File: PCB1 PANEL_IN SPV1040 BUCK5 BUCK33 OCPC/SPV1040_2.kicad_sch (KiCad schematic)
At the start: 14 parts, among them J2 SOLAR, U2 SPV1040TTR

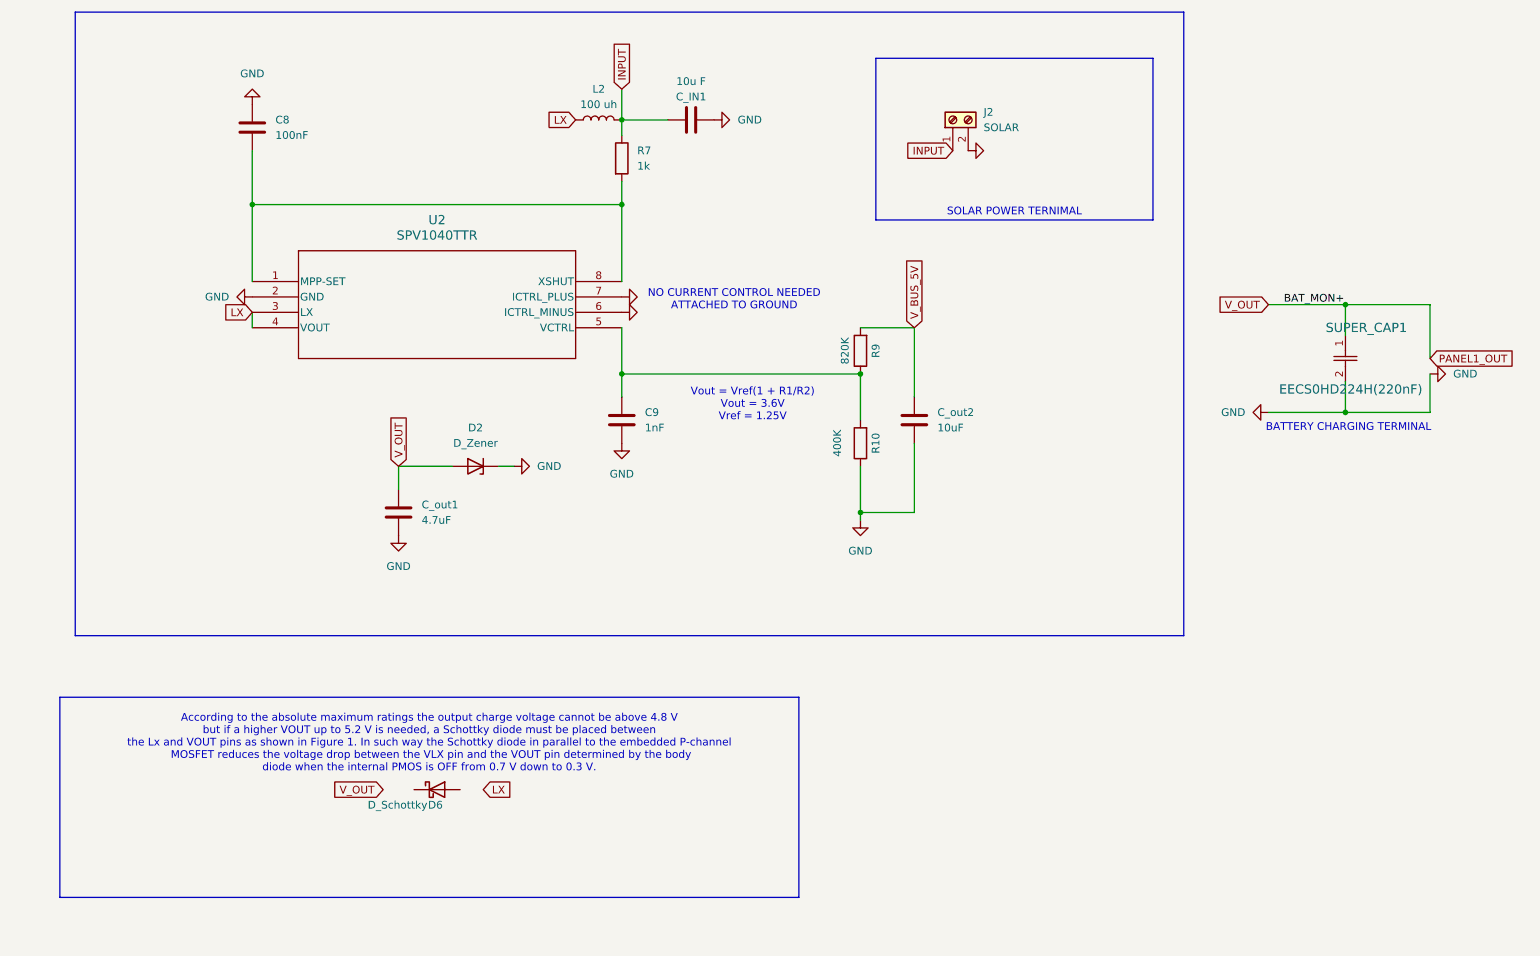
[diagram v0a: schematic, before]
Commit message: Changes
Added bucks from old work
and copied SPV
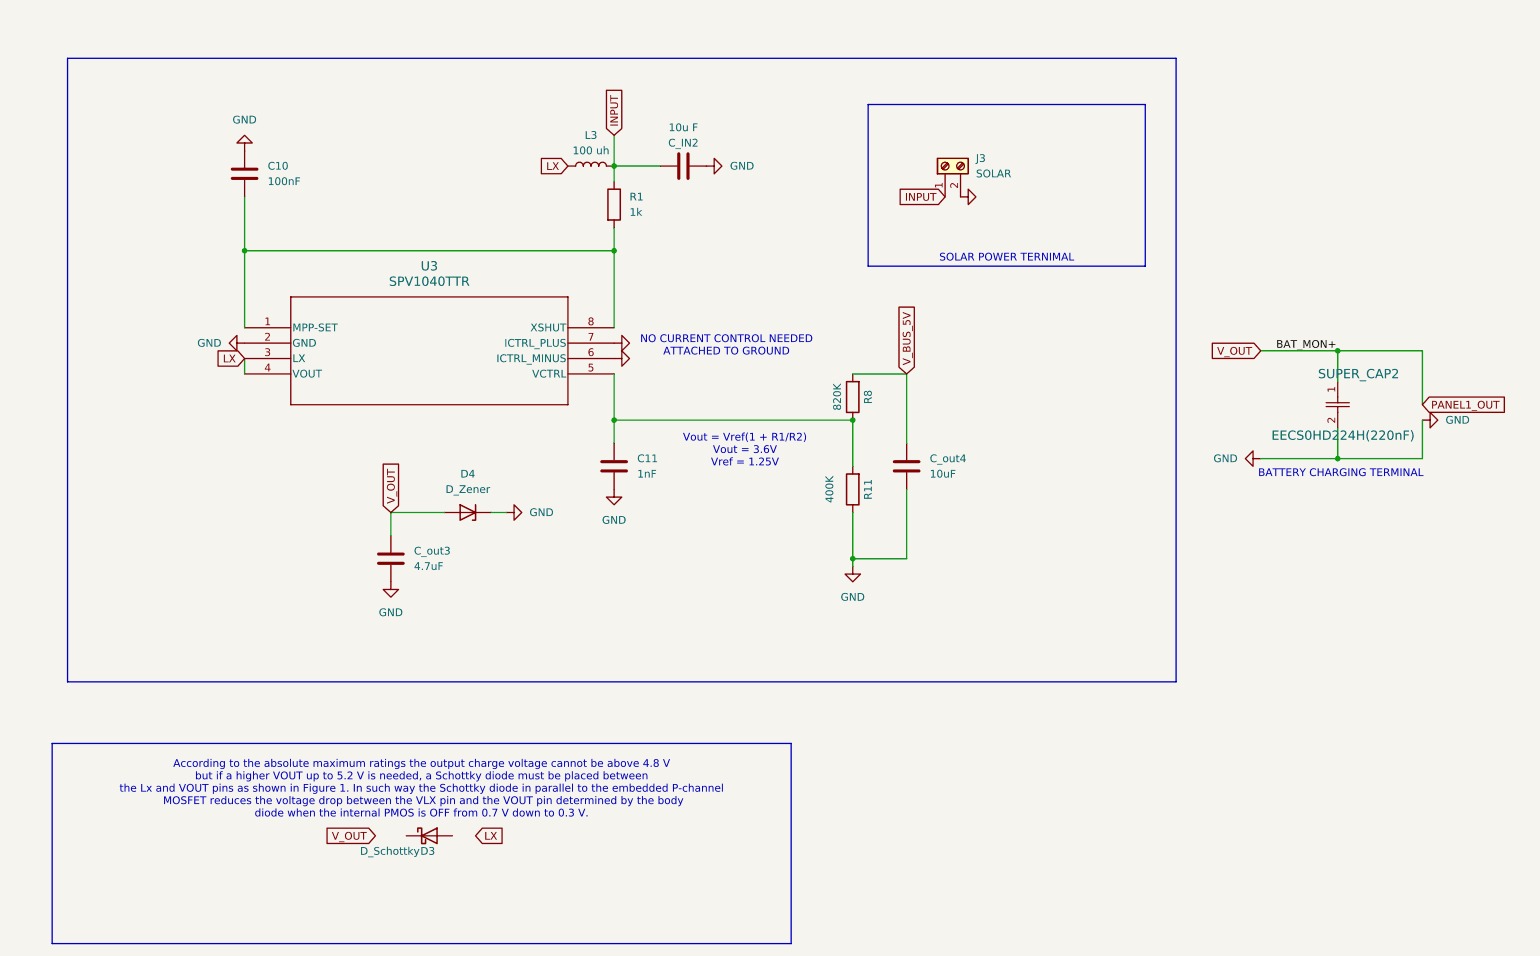
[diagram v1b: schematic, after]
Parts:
- removed C8: 100nF, Capacitor_SMD:C_0603_1608Metric, symbol Device:C
- removed C9: 1nF, Capacitor_SMD:C_0603_1608Metric, symbol Device:C
- removed C_IN1: 10u F, Capacitor_SMD:C_0603_1608Metric, symbol Device:C
- removed C_out1: 4.7uF, Capacitor_SMD:C_0603_1608Metric, symbol Device:C
- removed C_out2: 10uF, Capacitor_SMD:C_0603_1608Metric, symbol Device:C
- removed D2: D_Zener, Diode_SMD:D_1210_3225Metric, symbol Device:D_Zener
- removed D6: D_Schottky, symbol Device:D_Schottky
- removed J2: SOLAR, TerminalBlock_Phoenix:TerminalBlock_Phoenix_PT-1,5-2-5.0-H_1x02_P5.00mm_Horizontal, symbol Connector:Screw_Terminal_01x02
- removed L2: 100 uh, Inductor_SMD:L_Coilcraft_XAL6060-XXX, symbol Device:L
- removed R10: 400K, Resistor_SMD:R_0603_1608Metric, symbol Device:R
- removed R7: 1k, Resistor_SMD:R_0603_1608Metric, symbol Device:R
- removed R9: 820K, Resistor_SMD:R_0603_1608Metric, symbol Device:R
- removed SUPER_CAP1: EECS0HD224H(220nF), SPV1040T:CAP_EECS0_H_PAN, symbol 2024-06-08_06-57-05:super_capacitor
- removed U2: SPV1040TTR, SPV1040:SOP65P640X120-8N, symbol 2024-06-07_14-27-39:SPV1040TTR
- added C10: 100nF, Capacitor_SMD:C_0603_1608Metric, symbol Device:C
- added C11: 1nF, Capacitor_SMD:C_0603_1608Metric, symbol Device:C
- added C_IN2: 10u F, Capacitor_SMD:C_0603_1608Metric, symbol Device:C
- added C_out3: 4.7uF, Capacitor_SMD:C_0603_1608Metric, symbol Device:C
- added C_out4: 10uF, Capacitor_SMD:C_0603_1608Metric, symbol Device:C
- added D3: D_Schottky, symbol Device:D_Schottky
- added D4: D_Zener, Diode_SMD:D_1210_3225Metric, symbol Device:D_Zener
- added J3: SOLAR, TerminalBlock_Phoenix:TerminalBlock_Phoenix_PT-1,5-2-5.0-H_1x02_P5.00mm_Horizontal, symbol Connector:Screw_Terminal_01x02
- added L3: 100 uh, Inductor_SMD:L_Coilcraft_XAL6060-XXX, symbol Device:L
- added R1: 1k, Resistor_SMD:R_0603_1608Metric, symbol Device:R
- added R11: 400K, Resistor_SMD:R_0603_1608Metric, symbol Device:R
- added R8: 820K, Resistor_SMD:R_0603_1608Metric, symbol Device:R
- added SUPER_CAP2: EECS0HD224H(220nF), SPV1040T:CAP_EECS0_H_PAN, symbol 2024-06-08_06-57-05:super_capacitor
- added U3: SPV1040TTR, SPV1040:SOP65P640X120-8N, symbol 2024-06-07_14-27-39:SPV1040TTR
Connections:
- net GND: now also C10.1, C11.2, C_IN2.2, C_out3.1, C_out4.2, D4.1 (K), J3.2 (Pin_2), R11.1, SUPER_CAP2.2, U3.2 (GND), U3.6 (ICTRL_MINUS), U3.7 (ICTRL_PLUS)
- net INPUT: now also C_IN2.1, J3.1 (Pin_1), L3.2, R1.1
- net LX: now also L3.1, U3.3 (LX), U3.4 (VOUT)
- net PANEL1_OUT: now also C_out3.2, D4.2 (A), SUPER_CAP2.1
- net V_BUS_5V: now also C_out4.1, R8.2
- new net: C10.2, R1.2, U3.1 (MPP-SET), U3.8 (XSHUT)
- new net: C11.1, R11.2, R8.1, U3.5 (VCTRL)
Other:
- company: TEAM ANANT -> (none)
- title: SOLAR CHARGER -> (none)
